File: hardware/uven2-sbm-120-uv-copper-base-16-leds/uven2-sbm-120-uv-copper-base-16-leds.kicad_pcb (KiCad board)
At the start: 2 copper layers, 170 x 140 mm, 60 parts, among them J1 LED0+, J10 LED4-, J11 LED5+, J12 LED5-, J13 LED6+, J14 LED6-, J15 LED7+, J16 LED7-, J17 LED8+, J18 LED8-, J19 LED9+, J2 LED0-, J20 LED9-, J21 LED10+, J22 LED10-, J23 LED11+, J24 LED11-, J25 LED12+, J26 LED12-, J27 LED13+, J28 LED13-, J29 LED14+, J3 LED1+, J30 LED14-, J31 LED15+, J32 LED15-, J4 LED1-, J5 LED2+, J6 LED2-, J7 LED3+, J8 LED3-, J9 LED4+, U1 SBM-120-UV, U10 SBM-120-UV, U11 SBM-120-UV, U12 SBM-120-UV, U13 SBM-120-UV, U14 SBM-120-UV, U15 SBM-120-UV, U16 SBM-120-UV, U2 SBM-120-UV, U3 SBM-120-UV, U4 SBM-120-UV, U5 SBM-120-UV, U6 SBM-120-UV, U7 SBM-120-UV, U8 SBM-120-UV, U9 SBM-120-UV

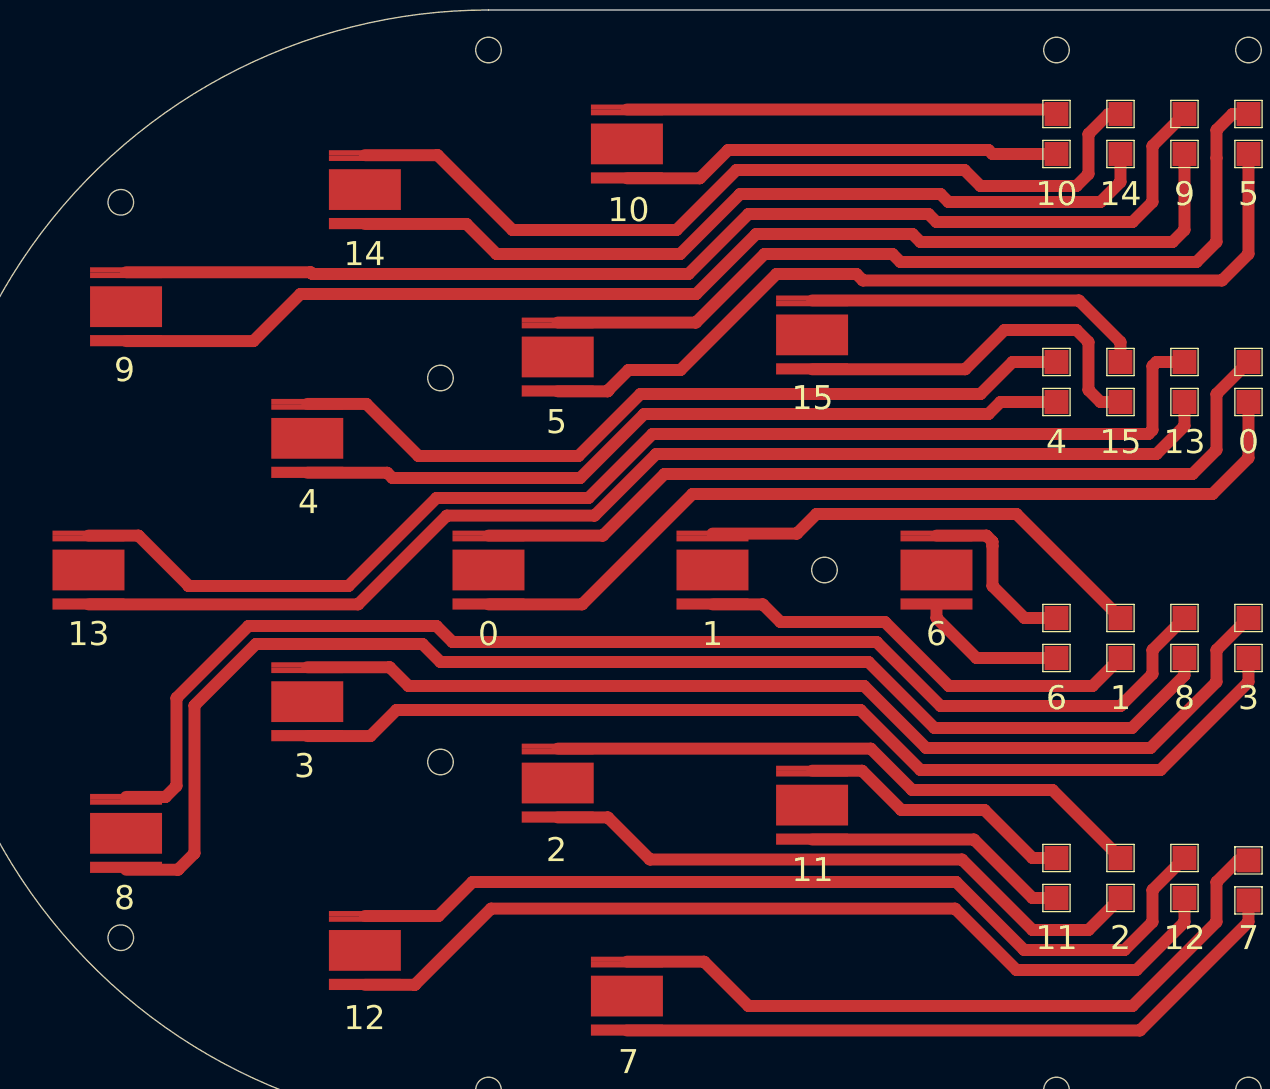
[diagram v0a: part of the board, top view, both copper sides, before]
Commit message: more mounting holes
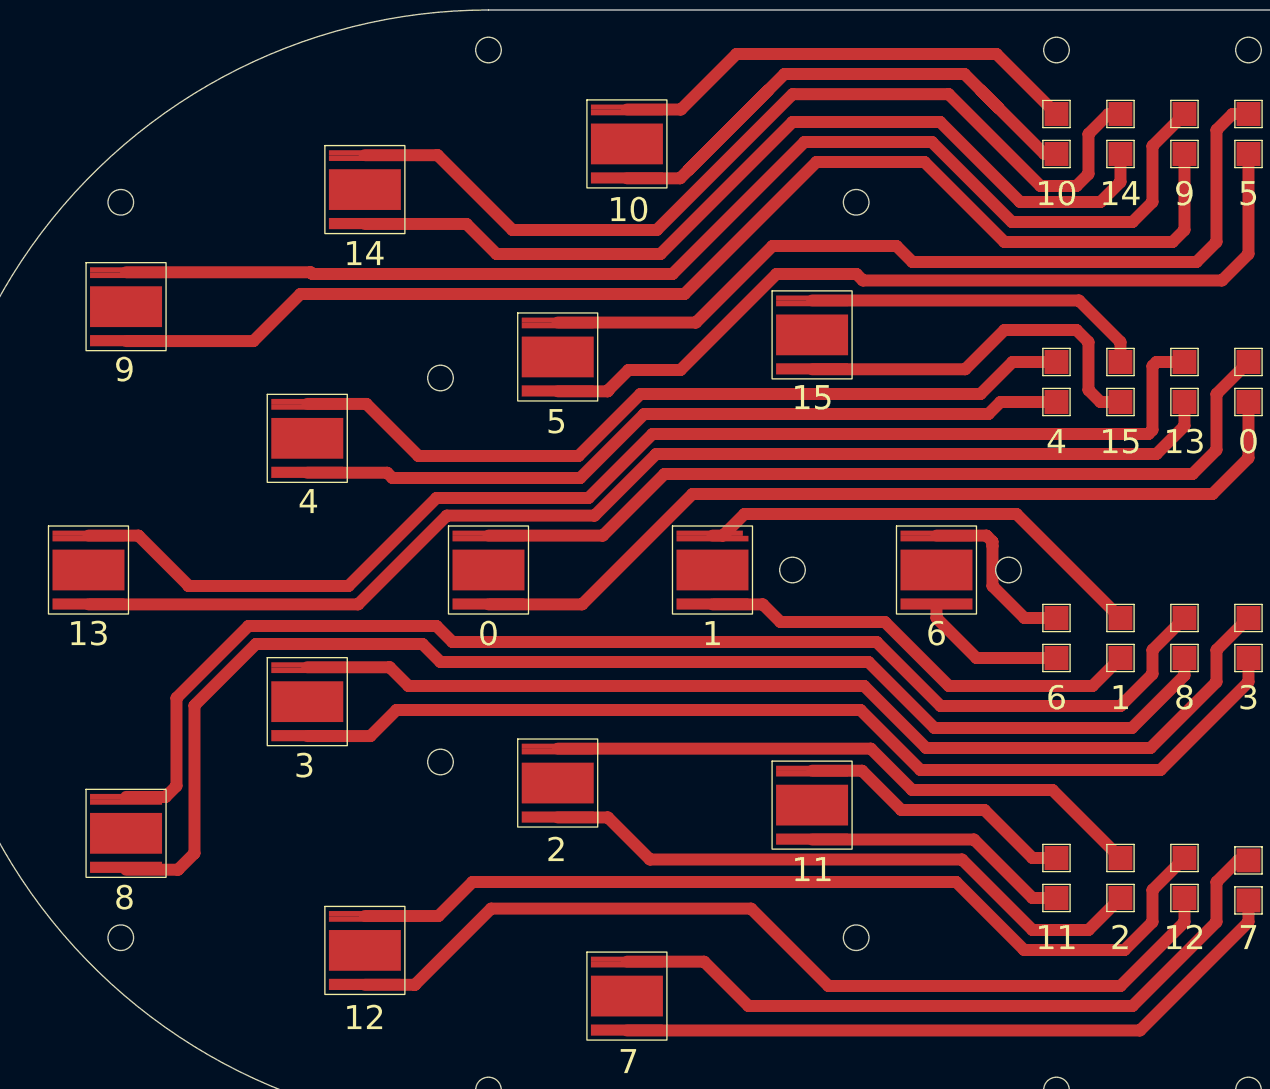
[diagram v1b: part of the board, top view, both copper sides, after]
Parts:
- added H13: MountingHole, MountingHole:MountingHole_3.2mm_M3, F.Cu at (166.0, 54.0)
- added H14: MountingHole, MountingHole:MountingHole_3.2mm_M3, F.Cu at (166.0, 146.0)
- added H15: MountingHole, MountingHole:MountingHole_3.2mm_M3, F.Cu at (185.0, 100.0)
- moved H9 4.00 mm to (158.0, 100.0)
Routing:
- net /LED10-: track 55.4 -> 80.6 mm
- net /LED14+: track 108.9 -> 116.8 mm
- net /LED9-: track 148.4 -> 155.8 mm
- net /LED14-: track 104.1 -> 111.5 mm
- net /LED9+: track 145.6 -> 153.1 mm
- net /LED10+: track 53.9 -> 59.7 mm
- net /LED12-: track 115.1 -> 116.7 mm
- net /LED5+: track 106.2 -> 107.0 mm

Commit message: with thermistors
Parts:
- added H16: MountingHole, MountingHole:MountingHole_3.2mm_M3, F.Cu at (172.1, 66.1)
- added H17: MountingHole, MountingHole:MountingHole_3.2mm_M3, F.Cu at (240.0, 38.0)
- added H18: MountingHole, MountingHole:MountingHole_3.2mm_M3, F.Cu at (172.1, 201.9)
- added H19: MountingHole, MountingHole:MountingHole_3.2mm_M3, F.Cu at (240.0, 230.0)
- added H20: MountingHole, MountingHole:MountingHole_3.2mm_M3, F.Cu at (144.0, 134.0)
- added J34: TEMP_LED0, TestPoint:TestPoint_Pad_2.0x2.0mm, F.Cu at (339.0, 211.0)
- added J35: TEMP_LED1, TestPoint:TestPoint_Pad_2.0x2.0mm, F.Cu at (338.9, 187.5)
- added J36: TEMP_LED2, TestPoint:TestPoint_Pad_2.0x2.0mm, F.Cu at (322.1, 187.5)
- added J37: TEMP_LED3, TestPoint:TestPoint_Pad_2.0x2.0mm, F.Cu at (326.3, 187.5)
- added J38: TEMP_LED4, TestPoint:TestPoint_Pad_2.0x2.0mm, F.Cu at (330.5, 211.0)
- added J39: TEMP_LED5, TestPoint:TestPoint_Pad_2.0x2.0mm, F.Cu at (322.1, 211.0)
- added J40: TEMP_LED6, TestPoint:TestPoint_Pad_2.0x2.0mm, F.Cu at (334.7, 187.5)
- added J41: TEMP_LED7, TestPoint:TestPoint_Pad_2.0x2.0mm, F.Cu at (309.5, 187.5)
- added J42: TEMP_LED8, TestPoint:TestPoint_Pad_2.0x2.0mm, F.Cu at (330.5, 187.5)
- added J43: TEMP_LED9, TestPoint:TestPoint_Pad_2.0x2.0mm, F.Cu at (317.9, 211.0)
- added J44: TEMP_LED10, TestPoint:TestPoint_Pad_2.0x2.0mm, F.Cu at (309.4, 211.0)
- added J45: TEMP_LED11, TestPoint:TestPoint_Pad_2.0x2.0mm, F.Cu at (317.9, 187.5)
- added J46: TEMP_LED12, TestPoint:TestPoint_Pad_2.0x2.0mm, F.Cu at (313.7, 187.5)
- added J47: TEMP_LED13, TestPoint:TestPoint_Pad_2.0x2.0mm, F.Cu at (334.8, 211.0)
- added J48: TEMP_LED14, TestPoint:TestPoint_Pad_2.0x2.0mm, F.Cu at (313.6, 211.0)
- added J49: TEMP_LED15, TestPoint:TestPoint_Pad_2.0x2.0mm, F.Cu at (326.3, 211.0)
- added J50: GND, TestPoint:TestPoint_Pad_2.0x2.0mm, F.Cu at (334.7, 214.7)
- added J51: GND, TestPoint:TestPoint_Pad_2.0x2.0mm, F.Cu at (330.5, 191.1)
- added J52: GND, TestPoint:TestPoint_Pad_2.0x2.0mm, F.Cu at (313.6, 214.7)
- added J53: GND, TestPoint:TestPoint_Pad_2.0x2.0mm, F.Cu at (339.0, 214.7)
- added J54: GND, TestPoint:TestPoint_Pad_2.0x2.0mm, F.Cu at (326.3, 191.1)
- added J55: GND, TestPoint:TestPoint_Pad_2.0x2.0mm, F.Cu at (313.7, 191.1)
- added J56: GND, TestPoint:TestPoint_Pad_2.0x2.0mm, F.Cu at (330.5, 214.7)
- added J57: GND, TestPoint:TestPoint_Pad_2.0x2.0mm, F.Cu at (322.1, 214.7)
- added J58: GND, TestPoint:TestPoint_Pad_2.0x2.0mm, F.Cu at (322.1, 191.1)
- added J59: GND, TestPoint:TestPoint_Pad_2.0x2.0mm, F.Cu at (326.3, 214.7)
- added J60: GND, TestPoint:TestPoint_Pad_2.0x2.0mm, F.Cu at (334.7, 191.1)
- added J61: GND, TestPoint:TestPoint_Pad_2.0x2.0mm, F.Cu at (338.9, 191.1)
- added J62: GND, TestPoint:TestPoint_Pad_2.0x2.0mm, F.Cu at (317.9, 191.1)
- added J63: GND, TestPoint:TestPoint_Pad_2.0x2.0mm, F.Cu at (309.4, 214.7)
- added J64: GND, TestPoint:TestPoint_Pad_2.0x2.0mm, F.Cu at (309.5, 191.1)
- added J65: GND, TestPoint:TestPoint_Pad_2.0x2.0mm, F.Cu at (317.8, 214.7)
- added TH1: NTC, Resistor_SMD:R_0805_2012Metric_Pad1.20x1.40mm_HandSolder, F.Cu at (233.7, 134.0)
- added TH10: NTC, Resistor_SMD:R_0805_2012Metric_Pad1.20x1.40mm_HandSolder, F.Cu at (188.5, 101.2)
- added TH11: NTC, Resistor_SMD:R_0805_2012Metric_Pad1.20x1.40mm_HandSolder, F.Cu at (251.0, 80.8)
- added TH12: NTC, Resistor_SMD:R_0805_2012Metric_Pad1.20x1.40mm_HandSolder, F.Cu at (274.3, 163.5)
- added TH13: NTC, Resistor_SMD:R_0805_2012Metric_Pad1.20x1.40mm_HandSolder, F.Cu at (218.3, 182.0)
- added TH14: NTC, Resistor_SMD:R_0805_2012Metric_Pad1.20x1.40mm_HandSolder, F.Cu at (183.8, 134.0)
- added TH15: NTC, Resistor_SMD:R_0805_2012Metric_Pad1.20x1.40mm_HandSolder, F.Cu at (218.3, 86.5)
- added TH16: NTC, Resistor_SMD:R_0805_2012Metric_Pad1.20x1.40mm_HandSolder, F.Cu at (274.3, 104.8)
- added TH2: NTC, Resistor_SMD:R_0805_2012Metric_Pad1.20x1.40mm_HandSolder, F.Cu at (261.8, 134.0)
- added TH3: NTC, Resistor_SMD:R_0805_2012Metric_Pad1.20x1.40mm_HandSolder, F.Cu at (242.3, 160.8)
- added TH4: NTC, Resistor_SMD:R_0805_2012Metric_Pad1.20x1.40mm_HandSolder, F.Cu at (211.0, 150.5)
- added TH5: NTC, Resistor_SMD:R_0805_2012Metric_Pad1.20x1.40mm_HandSolder, F.Cu at (211.0, 117.5)
- added TH6: NTC, Resistor_SMD:R_0805_2012Metric_Pad1.20x1.40mm_HandSolder, F.Cu at (242.3, 107.5)
- added TH7: NTC, Resistor_SMD:R_0805_2012Metric_Pad1.20x1.40mm_HandSolder, F.Cu at (289.8, 134.0)
- added TH8: NTC, Resistor_SMD:R_0805_2012Metric_Pad1.20x1.40mm_HandSolder, F.Cu at (251.0, 187.5)
- added TH9: NTC, Resistor_SMD:R_0805_2012Metric_Pad1.20x1.40mm_HandSolder, F.Cu at (188.3, 167.0)
- moved H3 138.3 mm to (337.0, 230.0)
- moved H6 137.4 mm to (312.0, 230.0)
- moved H1 124.7 mm to (175.0, 134.0)
- moved H10 124.7 mm to (234.0, 110.0)
- moved H11 124.7 mm to (234.0, 158.0)
- moved H12 124.7 mm to (194.1, 88.0)
- moved H13 124.7 mm to (286.0, 88.0)
- moved H14 124.7 mm to (286.0, 180.0)
- moved H5 124.7 mm to (240.0, 69.0)
- moved H7 124.7 mm to (240.0, 199.0)
- moved H8 124.7 mm to (194.1, 180.0)
- moved U1 124.7 mm to (240.0, 134.0)
- moved U11 124.7 mm to (257.3, 80.7)
- moved U13 124.7 mm to (224.6, 181.6)
- moved U14 124.7 mm to (190.0, 134.0)
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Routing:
- net GND: track 0.00 -> 3752.7 mm
- net Net-(J49-Pad1): track 0.00 -> 323.9 mm
- net Net-(J44-Pad1): track 0.00 -> 322.1 mm
- net Net-(J40-Pad1): track 0.00 -> 305.7 mm
- net Net-(J39-Pad1): track 0.00 -> 299.3 mm
- net Net-(J48-Pad1): track 0.00 -> 298.7 mm
- net Net-(J35-Pad1): track 0.00 -> 288.0 mm
- net Net-(J34-Pad1): track 0.00 -> 255.6 mm
- net Net-(J38-Pad1): track 0.00 -> 253.0 mm
- net Net-(J43-Pad1): track 0.00 -> 248.9 mm
- net Net-(J47-Pad1): track 0.00 -> 218.0 mm
- net Net-(J45-Pad1): track 0.00 -> 187.5 mm
- net Net-(J42-Pad1): track 0.00 -> 173.9 mm
- net Net-(J36-Pad1): track 0.00 -> 164.8 mm
- net Net-(J37-Pad1): track 0.00 -> 163.9 mm
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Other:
- board size 170 x 140 mm -> 201 x 200 mm

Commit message: ordered on jlcpcb
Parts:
- added FID1: Fiducial, Fiducial:Fiducial_1mm_Dia_2.54mm_Outer_CopperTop, F.Cu at (155.0, 134.0)
- added FID2: Fiducial, Fiducial:Fiducial_1mm_Dia_2.54mm_Outer_CopperTop, F.Cu at (330.0, 224.0)
- added FID3: Fiducial, Fiducial:Fiducial_1mm_Dia_2.54mm_Outer_CopperTop, F.Cu at (330.0, 44.0)
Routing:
- net GND: track 3752.7 -> 3749.3 mm
- net /LED10-: track 61.8 -> 63.2 mm
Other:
- board text added: "DH"
